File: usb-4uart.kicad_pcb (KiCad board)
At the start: 2 copper layers, 25 x 65 mm, 49 parts, among them J1 Conn_02x05_Odd_Even, X1 24MHz

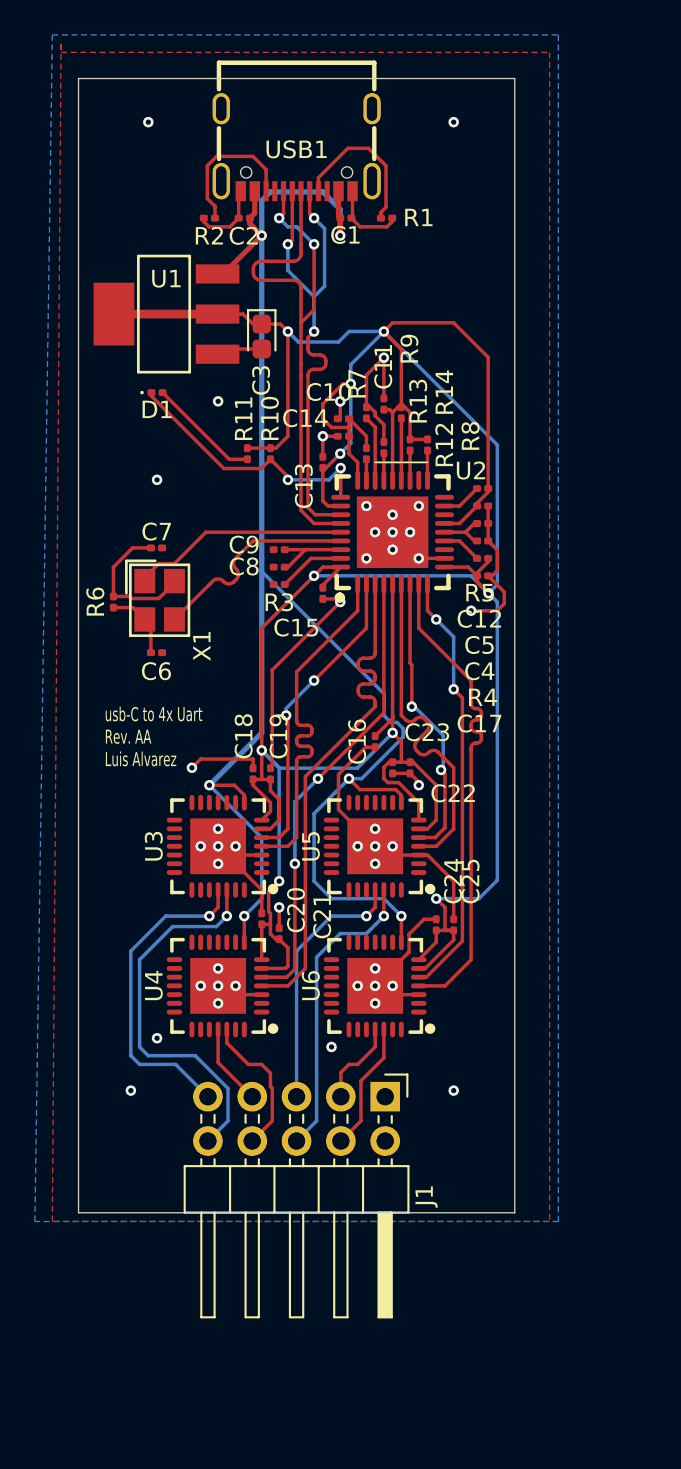
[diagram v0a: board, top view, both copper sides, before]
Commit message: -updated layout and traces -relocated caps -rotated devices -usb paths more even now
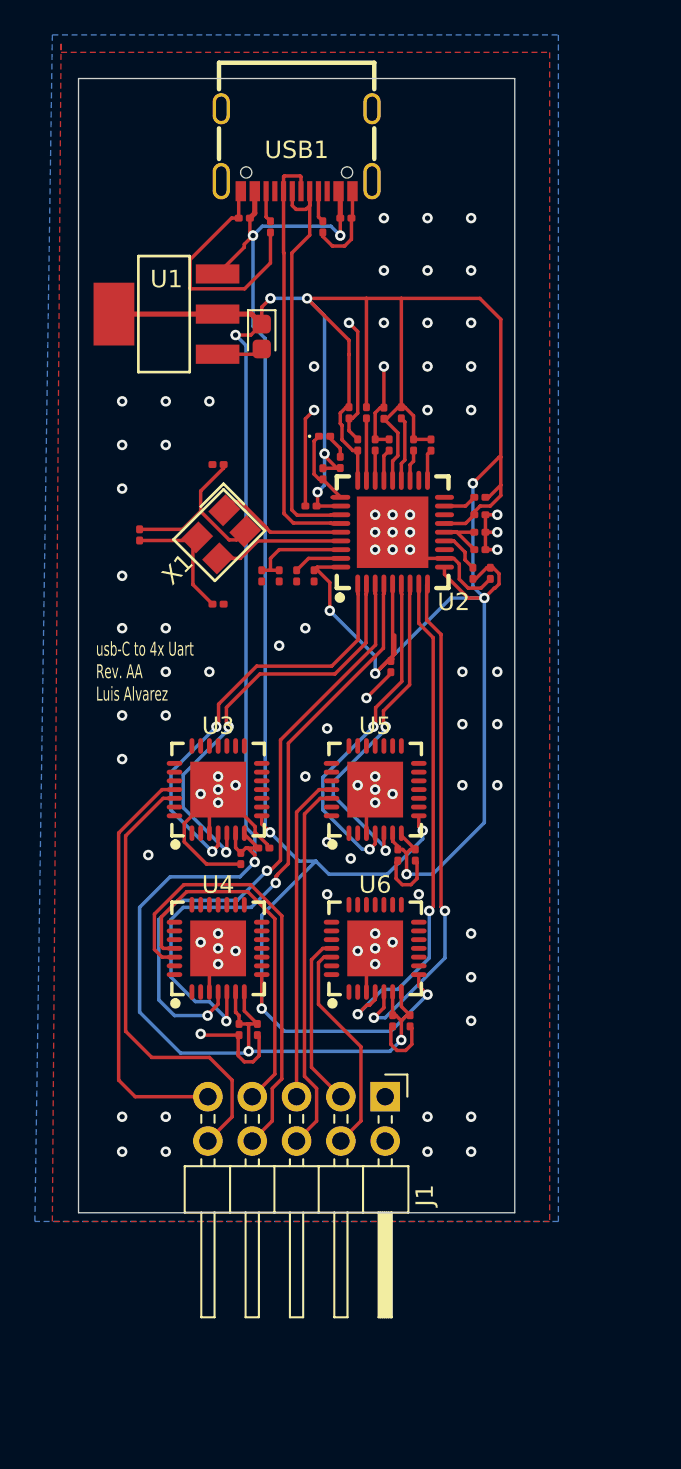
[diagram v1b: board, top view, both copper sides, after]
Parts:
- moved D1 9.92 mm to (34.1, 39.0)
- moved C25 6.52 mm to (38.0, 72.5), turned to -90 degrees
- moved C20 6.35 mm to (30.2, 73.0), turned to -90 degrees
- moved C21 5.96 mm to (29.2, 73.0), turned to -90 degrees
- moved C7 5.94 mm to (28.0, 40.6), turned to 180 degrees
- moved C24 5.70 mm to (39.0, 72.5), turned to -90 degrees
- moved R11 5.34 mm to (35.0, 40.5), turned to 90 degrees
- moved X1 5.17 mm to (28.2, 44.6)
- moved C19 5.14 mm to (29.3, 63.2), turned to -90 degrees
- moved C22 5.01 mm to (39.3, 63.0)
- moved C23 5.01 mm to (38.3, 63.0)
- moved C13 4.49 mm to (37.5, 37.7)
- moved C6 4.49 mm to (28.0, 48.6)
- moved C14 4.41 mm to (33.3, 43.0)
- moved C16 4.39 mm to (37.9, 52.2)
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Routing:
- net TX2: track 8.40 -> 25.7 mm
- net +3.3V: track 214.8 -> 232.1 mm, vias 10 -> 13
- net RX2: track 4.66 -> 21.0 mm
- net +5V: track 99.4 -> 85.5 mm
- net SUSP_IND: track 15.5 -> 4.87 mm, vias 2 -> 0
- net USB_IN+: track 34.6 -> 24.7 mm, vias 2 -> 0
- net D2-: track 26.3 -> 35.8 mm
- net Net-(USB1-CC1): track 8.87 -> 1.83 mm
- net D1-: track 17.7 -> 24.5 mm
- net Net-(USB1-CC2): track 8.33 -> 1.83 mm
- net D2+: track 29.4 -> 35.9 mm, vias 0 -> 2
- net RX1: track 18.4 -> 23.9 mm, vias 1 -> 0
- net TX4: track 7.41 -> 12.6 mm
- net Net-(D1-A): track 6.44 -> 1.42 mm
- net RX4: track 4.96 -> 9.97 mm
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
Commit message: updated cp2102 vias updated crystal circuitry updated 3v3 joints
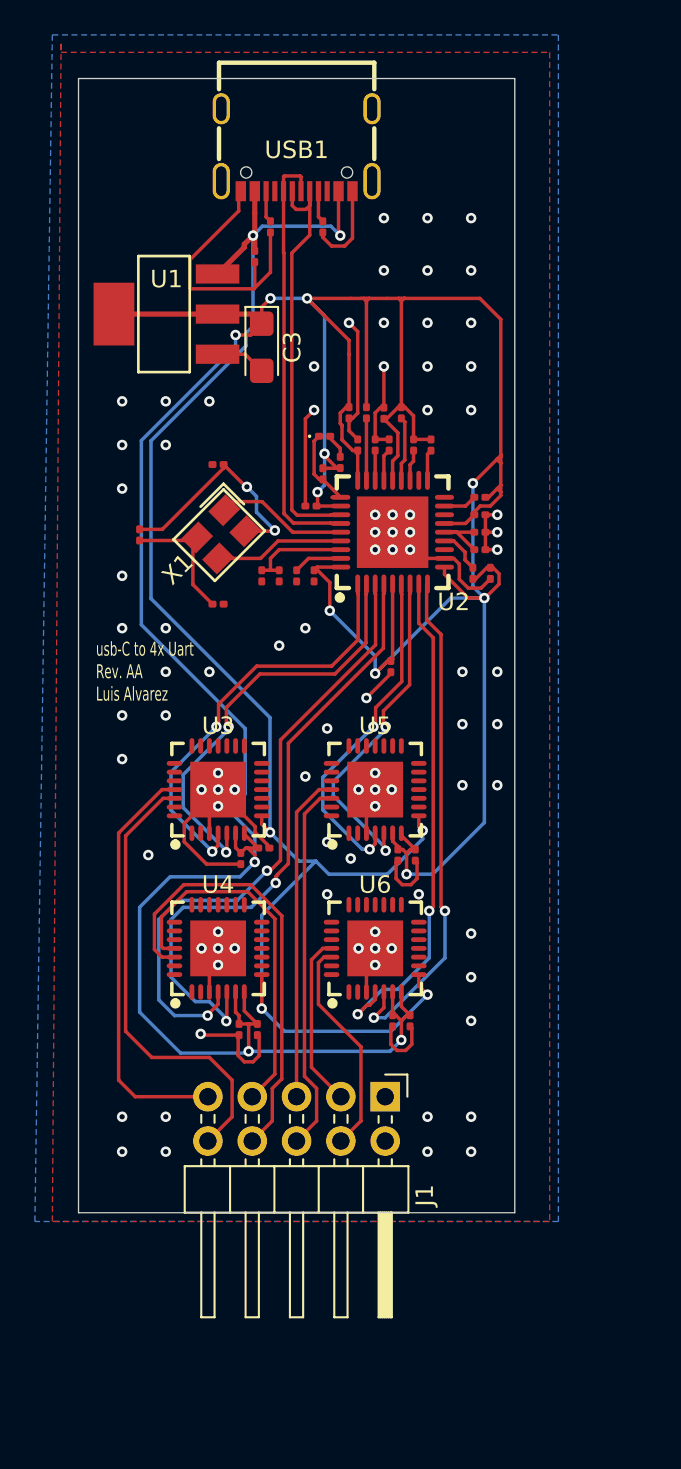
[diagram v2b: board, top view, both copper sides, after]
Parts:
- removed C2: 100nF, Capacitor_SMD:C_0201_0603Metric
- C1: value 100nF -> 10u
- C3: footprint Capacitor_Tantalum_SMD:CP_EIA-1608-08_AVX-J -> Capacitor_Tantalum_SMD:CP_EIA-3216-18_Kemet-A
- moved C1 5.66 mm to (30.1, 28.7), turned to -90 degrees
- moved C3 0.61 mm to (30.5, 33.9)
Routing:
- net +5V: track 85.5 -> 91.3 mm
- net +3.3V: track 232.1 -> 236.6 mm
- net Net-(C7-Pad1): track 10.6 -> 13.2 mm, vias 0 -> 2
- net GND: track 90.2 -> 92.1 mm

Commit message: fixed crystal
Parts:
- moved C6 3.73 mm to (25.2, 46.1), turned to 180 degrees
- moved C7 1.70 mm to (29.6, 41.3), turned to 90 degrees
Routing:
- net Net-(C6-Pad1): track 7.76 -> 5.25 mm
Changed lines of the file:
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@@
 			(sketchpadsonfab no)
 			(subtractmaskfromsilk yes)
-			(outputformat 1)
+			(outputformat 4)
 			(mirror no)
 			(drillshape 0)
@@
 	(footprint "Capacitor_SMD:C_0201_0603Metric"
 		(layer "F.Cu")
-		(at 27.996776 48.621142)
+		(at 25.2 46.15 180)
 		(descr "Capacitor SMD 0201 (0603 Metric), square (rectangular) end terminal, IPC_7351 nominal, (Body size source: https://www.vishay.com/docs/20052/crcw0201e3.pdf), generated with kicad-footprint-generator")
 		(tags "capacitor")
 		(property "Reference" "C6"
-			(at -2.32 0 0)
+			(at -2.32 0 360)
 			(layer "F.SilkS")
 			(hide yes)
@@
 		)
 		(property "Value" "12pF"
-			(at 0 1.05 0)
+			(at 0 1.05 360)
 			(layer "F.Fab")
 			(effects
@@
 		)
 		(property "Footprint" "Capacitor_SMD:C_0201_0603Metric"
-			(at 0 0 0)
+			(at 0 0 180)
 			(unlocked yes)
 			(layer "F.Fab")
@@
 		)
 		(property "Datasheet" ""
-			(at 0 0 0)
+			(at 0 0 180)
 			(unlocked yes)
 			(layer "F.Fab")
@@
 		)
 		(property "Description" "Unpolarized capacitor"
-			(at 0 0 0)
+			(at 0 0 180)
 			(unlocked yes)
 			(layer "F.Fab")
@@
 		(attr smd)
 		(fp_line
-			(start -0.7 -0.35)
-			(end 0.7 -0.35)
+			(start 0.7 0.35)
+			(end -0.7 0.35)
 			(stroke
 				(width 0.05)
@@
 		)
 		(fp_line
-			(start -0.7 0.35)
-			(end -0.7 -0.35)
+			(start 0.7 -0.35)
+			(end 0.7 0.35)
 			(stroke
 				(width 0.05)
@@
 		)
 		(fp_line
-			(start 0.7 -0.35)
-			(end 0.7 0.35)
+			(start -0.7 0.35)
+			(end -0.7 -0.35)
 			(stroke
 				(width 0.05)
@@
 		)
 		(fp_line
-			(start 0.7 0.35)
-			(end -0.7 0.35)
+			(start -0.7 -0.35)
+			(end 0.7 -0.35)
 			(stroke
 				(width 0.05)
@@
 		)
 		(fp_line
-			(start -0.3 -0.15)
-			(end 0.3 -0.15)
+			(start 0.3 0.15)
+			(end -0.3 0.15)
 			(stroke
 				(width 0.1)
@@
 		)
 		(fp_line
-			(start -0.3 0.15)
-			(end -0.3 -0.15)
+			(start 0.3 -0.15)
+			(end 0.3 0.15)
 			(stroke
 				(width 0.1)
@@
 		)
 		(fp_line
-			(start 0.3 -0.15)
-			(end 0.3 0.15)
+			(start -0.3 0.15)
+			(end -0.3 -0.15)
 			(stroke
 				(width 0.1)
@@
 		)
 		(fp_line
-			(start 0.3 0.15)
-			(end -0.3 0.15)
+			(start -0.3 -0.15)
+			(end 0.3 -0.15)
 			(stroke
 				(width 0.1)
@@
 		)
 		(fp_text user "${REFERENCE}"
-			(at 0 -0.68 0)
+			(at 0 -0.68 360)
 			(layer "F.Fab")
 			(effects
@@
 		)
 		(pad "" smd roundrect
-			(at -0.345 0)
+			(at -0.345 0 180)
 			(size 0.318 0.36)
 			(layers "F.Paste")
@@
 		)
 		(pad "" smd roundrect
-			(at 0.345 0)
+			(at 0.345 0 180)
 			(size 0.318 0.36)
 			(layers "F.Paste")
@@
 		)
 		(pad "1" smd roundrect
-			(at -0.32 0)
+			(at -0.32 0 180)
 			(size 0.46 0.4)
 			(layers "F.Cu" "F.Mask")
@@
 		)
 		(pad "2" smd roundrect
-			(at 0.32 0)
+			(at 0.32 0 180)
 			(size 0.46 0.4)
 			(layers "F.Cu" "F.Mask")
@@
 		(at 28.176776 44.621142 -90)
 		(property "Reference" "X1"
-			(at 2 2.5 45)
+			(at 2.828858 1.576776 45)
 			(layer "F.SilkS")
 			(effects
@@
 	(footprint "Capacitor_SMD:C_0201_0603Metric"
 		(layer "F.Cu")
-		(at 27.996776 40.621142 180)
+		(at 29.55 41.305 90)
 		(descr "Capacitor SMD 0201 (0603 Metric), square (rectangular) end terminal, IPC_7351 nominal, (Body size source: https://www.vishay.com/docs/20052/crcw0201e3.pdf), generated with kicad-footprint-generator")
 		(tags "capacitor")
 		(property "Reference" "C7"
-			(at 1.82 0 0)
+			(at 1.82 0 90)
 			(layer "F.SilkS")
 			(hide yes)
@@
 		)
 		(property "Value" "12pF"
-			(at 0 1.05 0)
+			(at 0 1.05 90)
 			(layer "F.Fab")
 			(effects
@@
 		)
 		(property "Footprint" "Capacitor_SMD:C_0201_0603Metric"
-			(at 0 0 180)
+			(at 0 0 90)
 			(unlocked yes)
 			(layer "F.Fab")
@@
 		)
 		(property "Datasheet" ""
-			(at 0 0 180)
+			(at 0 0 90)
 			(unlocked yes)
 			(layer "F.Fab")
@@
 		)
 		(property "Description" "Unpolarized capacitor"
-			(at 0 0 180)
+			(at 0 0 90)
 			(unlocked yes)
 			(layer "F.Fab")
@@
 		(attr smd)
 		(fp_line
-			(start 0.7 0.35)
-			(end -0.7 0.35)
+			(start 0.7 -0.35)
+			(end 0.7 0.35)
 			(stroke
 				(width 0.05)
@@
 		)
 		(fp_line
-			(start 0.7 -0.35)
-			(end 0.7 0.35)
+			(start -0.7 -0.35)
+			(end 0.7 -0.35)
 			(stroke
 				(width 0.05)
@@
 		)
 		(fp_line
-			(start -0.7 0.35)
-			(end -0.7 -0.35)
+			(start 0.7 0.35)
+			(end -0.7 0.35)
 			(stroke
 				(width 0.05)
@@
 		)
 		(fp_line
-			(start -0.7 -0.35)
-			(end 0.7 -0.35)
+			(start -0.7 0.35)
+			(end -0.7 -0.35)
 			(stroke
 				(width 0.05)
@@
 		)
 		(fp_line
-			(start 0.3 0.15)
-			(end -0.3 0.15)
+			(start 0.3 -0.15)
+			(end 0.3 0.15)
 			(stroke
 				(width 0.1)
@@
 		)
 		(fp_line
-			(start 0.3 -0.15)
-			(end 0.3 0.15)
+			(start -0.3 -0.15)
+			(end 0.3 -0.15)
 			(stroke
 				(width 0.1)
@@
 		)
 		(fp_line
-			(start -0.3 0.15)
-			(end -0.3 -0.15)
+			(start 0.3 0.15)
+			(end -0.3 0.15)
 			(stroke
 				(width 0.1)
@@
 		)
 		(fp_line
-			(start -0.3 -0.15)
-			(end 0.3 -0.15)
+			(start -0.3 0.15)
+			(end -0.3 -0.15)
 			(stroke
 				(width 0.1)
@@
 		)
 		(fp_text user "${REFERENCE}"
-			(at 0 -0.68 0)
+			(at 0 -0.68 90)
 			(layer "F.Fab")
 			(effects
@@
 		)
 		(pad "" smd roundrect
-			(at -0.345 0 180)
+			(at -0.345 0 90)
 			(size 0.318 0.36)
 			(layers "F.Paste")
@@
 		)
 		(pad "" smd roundrect
-			(at 0.345 0 180)
+			(at 0.345 0 90)
 			(size 0.318 0.36)
 			(layers "F.Paste")
@@
 		)
 		(pad "1" smd roundrect
-			(at -0.32 0 180)
+			(at -0.32 0 90)
 			(size 0.46 0.4)
 			(layers "F.Cu" "F.Mask")
@@
 		)
 		(pad "2" smd roundrect
-			(at 0.32 0 180)
+			(at 0.32 0 90)
 			(size 0.46 0.4)
 			(layers "F.Cu" "F.Mask")
@@
 	)
 	(segment
-		(start 26.554694 45.041142)
-		(end 26.554694 47.49906)
-		(width 0.2)
-		(layer "F.Cu")
-		(net 10)
-	)
-	(segment
-		(start 26.797918 44.797918)
-		(end 26.554694 45.041142)
+		(start 25.52 46.075836)
+		(end 26.797918 44.797918)
 		(width 0.2)
 		(layer "F.Cu")
@@
 	)
 	(segment
-		(start 26.554694 47.49906)
-		(end 27.676776 48.621142)
+		(start 25.52 46.15)
+		(end 25.52 46.075836)
 		(width 0.2)
 		(layer "F.Cu")
@@
 	)
 	(segment
-		(start 29.595634 41.9)
-		(end 28.316776 40.621142)
+		(start 29.55 41.625)
+		(end 28.125 41.625)
 		(width 0.2)
 		(layer "F.Cu")
@@
 	)
 	(segment
-		(start 29.65 41.9)
-		(end 29.595634 41.9)
+		(start 30.225 41.625)
+		(end 30.55 41.95)
 		(width 0.2)
 		(layer "F.Cu")
@@
 	)
 	(segment
-		(start 29.555634 44.444366)
-		(end 31.205634 44.444366)
+		(start 25.415 44.335)
+		(end 23.5 44.335)
 		(width 0.2)
 		(layer "F.Cu")
@@
 	)
 	(segment
-		(start 28.316776 40.821141)
-		(end 28.316776 40.621142)
+		(start 29.555634 44.444366)
+		(end 31.205634 44.444366)
 		(width 0.2)
 		(layer "F.Cu")
@@
 	)
 	(segment
-		(start 24.802917 44.335)
-		(end 28.316776 40.821141)
+		(start 29.55 41.625)
+		(end 30.225 41.625)
 		(width 0.2)
 		(layer "F.Cu")
@@
 	)
 	(segment
-		(start 31.205634 44.444366)
-		(end 31.25 44.4)
+		(start 28.125 41.625)
+		(end 25.415 44.335)
 		(width 0.2)
 		(layer "F.Cu")
@@
 	)
 	(segment
-		(start 23.5 44.335)
-		(end 24.802917 44.335)
+		(start 31.205634 44.444366)
+		(end 31.25 44.4)
 		(width 0.2)
 		(layer "F.Cu")
@@
 	)
 	(via
-		(at 29.65 41.9)
+		(at 30.55 41.95)
 		(size 0.6)
 		(drill 0.3)
@@
 	)
 	(segment
-		(start 30.2 43.35)
-		(end 31.25 44.4)
+		(start 30.55 41.95)
+		(end 30.9 42.3)
 		(width 0.2)
 		(layer "B.Cu")
@@
 	)
 	(segment
-		(start 30.2 42.45)
-		(end 30.2 43.35)
+		(start 30.9 44.05)
+		(end 31.25 44.4)
 		(width 0.2)
 		(layer "B.Cu")
@@
 	)
 	(segment
-		(start 29.65 41.9)
-		(end 30.2 42.45)
+		(start 30.9 42.3)
+		(end 30.9 44.05)
 		(width 0.2)
 		(layer "B.Cu")

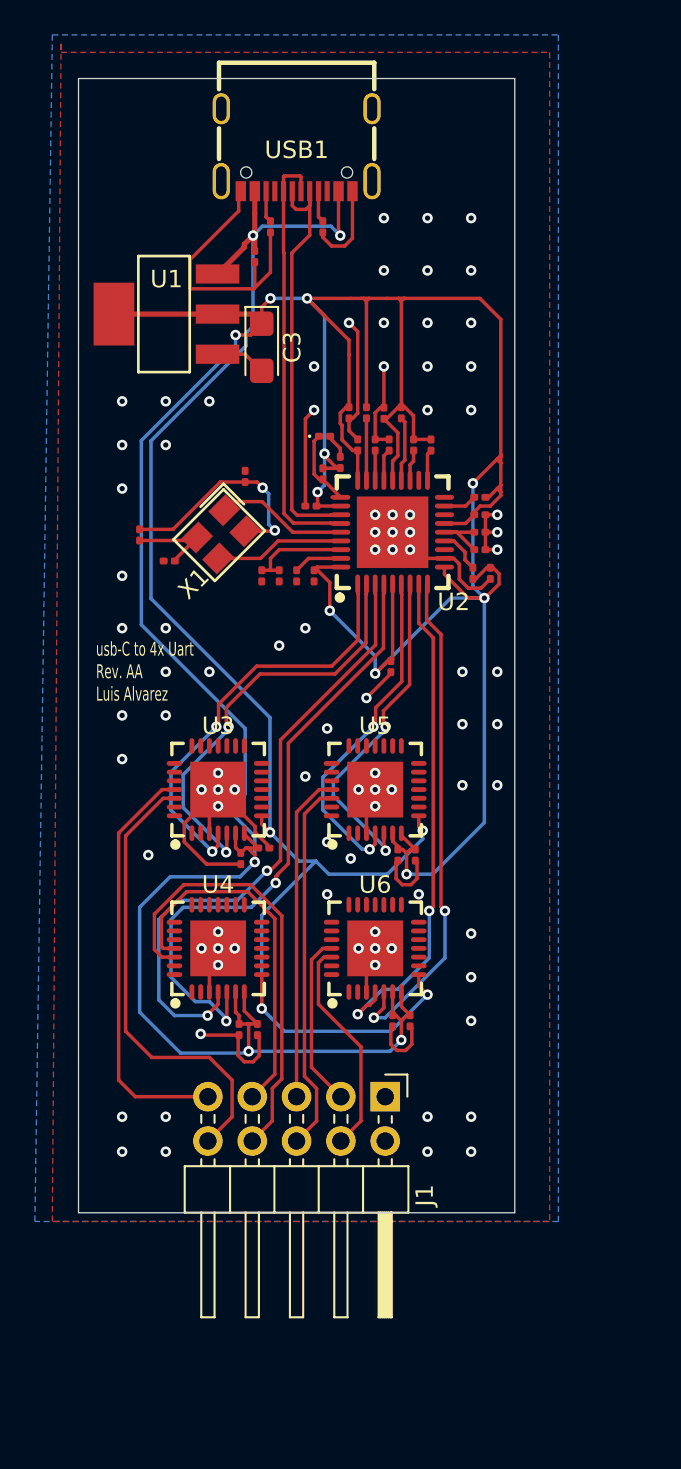
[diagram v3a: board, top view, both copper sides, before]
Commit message: -updated to kicad 9.0.1 -reworked layout with correct footprints
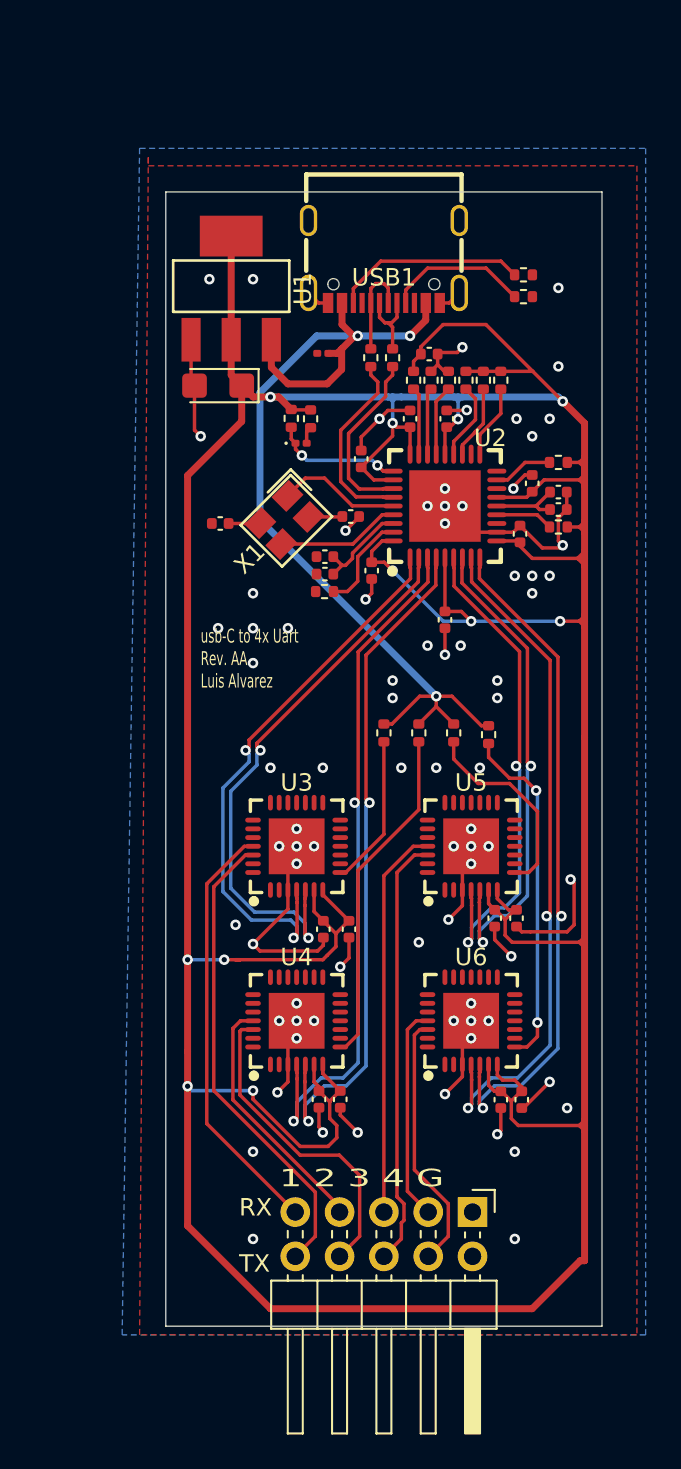
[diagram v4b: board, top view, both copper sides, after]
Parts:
- removed R6: 1M, Resistor_SMD:R_0201_0603Metric
- added R15: 20, Resistor_SMD:R_0402_1005Metric, F.Cu at (36.8, 34.5)
- added R16: 20, Resistor_SMD:R_0402_1005Metric, F.Cu at (38.0, 34.5)
- added R17: 4.7k, Resistor_SMD:R_0402_1005Metric, F.Cu at (41.5, 56.0)
- added R18: 4.7k, Resistor_SMD:R_0402_1005Metric, F.Cu at (43.5, 56.1)
- added R19: 4.7k, Resistor_SMD:R_0402_1005Metric, F.Cu at (39.5, 56.0)
- added R20: 4.7k, Resistor_SMD:R_0402_1005Metric, F.Cu at (37.5, 56.0)
- C10, C11, C12, C13, C14, C15, C16, C17, C18, C19, C20, C21, C22, C23, C24, C25, C4, C5, C6, C7, C8, C9: footprint Capacitor_SMD:C_0201_0603Metric -> Capacitor_SMD:C_0402_1005Metric
- R1, R10, R11, R12, R13, R14, R2, R3, R4, R5, R7, R8, R9: footprint Resistor_SMD:R_0201_0603Metric -> Resistor_SMD:R_0402_1005Metric
- moved R2 14.8 mm to (45.5, 29.8), turned to 0 degrees
- moved C14 12.7 mm to (46.0, 41.7), turned to 90 degrees
- moved R1 12.2 mm to (45.5, 31.0), turned to 0 degrees
- moved C15 12.0 mm to (45.3, 44.6), turned to 90 degrees
- moved C16 12.0 mm to (36.2, 40.3), turned to 90 degrees
- moved C11 11.2 mm to (41.0, 49.5), turned to -90 degrees
- moved J1 8.29 mm to (42.6, 83.5)
- moved USB1 8.13 mm to (37.5, 29.0)
- moved C24 7.84 mm to (45.4, 77.0)
- moved C25 7.67 mm to (44.2, 77.0)
- moved U6 6.89 mm to (42.5, 72.5)
- moved C22 6.84 mm to (45.1, 66.6)
- moved C17 6.80 mm to (36.8, 46.7)
- moved C12 6.80 mm to (39.0, 38.0), turned to 90 degrees
- moved C1 6.78 mm to (34.0, 34.2), turned to 180 degrees
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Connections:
- U3 pad 8: +5V -> Net-(U3-VBUS)
- U4 pad 8: +5V -> Net-(U4-VBUS)
- U5 pad 8: +5V -> Net-(U5-VBUS)
- U6 pad 8: +5V -> Net-(U6-VBUS)
- USB1 pad A6: USB_IN+ -> Net-(USB1-DP1)
- USB1 pad A7: USB_IN- -> Net-(USB1-DN1)
- USB1 pad B6: USB_IN+ -> Net-(USB1-DP1)
- USB1 pad B7: USB_IN- -> Net-(USB1-DN1)
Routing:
- net +3.3V: track 236.6 -> 282.7 mm, vias 13 -> 11
- net +5V: track 91.3 -> 56.6 mm, vias 6 -> 3
- net Net-(U6-VBUS): track 0.00 -> 20.0 mm, vias 0 -> 2
- net Net-(U4-VBUS): track 0.00 -> 19.5 mm
- net GND: track 92.1 -> 77.7 mm, vias 91 -> 79
- net USB_IN-: track 24.5 -> 10.3 mm
- net USB_IN+: track 24.7 -> 11.0 mm
- net Net-(U5-VBUS): track 0.00 -> 11.5 mm
- net Net-(C7-Pad1): track 12.8 -> 1.95 mm, vias 2 -> 0
- net D4+: track 29.1 -> 39.0 mm
- net D4-: track 29.1 -> 39.0 mm
- net Net-(USB1-CC2): track 1.83 -> 11.0 mm
- net D3-: track 19.5 -> 28.5 mm
- net D3+: track 19.5 -> 28.5 mm
- net Net-(U3-VBUS): track 0.00 -> 8.71 mm
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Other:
- board text added: "1 2 3 4 G"
- board text added: "RX TX"
